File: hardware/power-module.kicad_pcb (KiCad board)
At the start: 2 copper layers, 33 x 82 mm, 35 parts, among them CN1 WJ2EDGRC-5.08-2P, K1 SRD-03VDC-SL-C, K2 SRD-03VDC-SL-C, K3 SRD-03VDC-SL-C, K4 SRD-03VDC-SL-C, Q1 BC547C, Q2 BC547C, U1 MIC5205-3.3YM5-MS, U2 PM254-2-05-W-8.5, U3 CC6903SO-10A, U4 ESP32-C3-MINI-1, U5 XC6206P332MR_C5148692

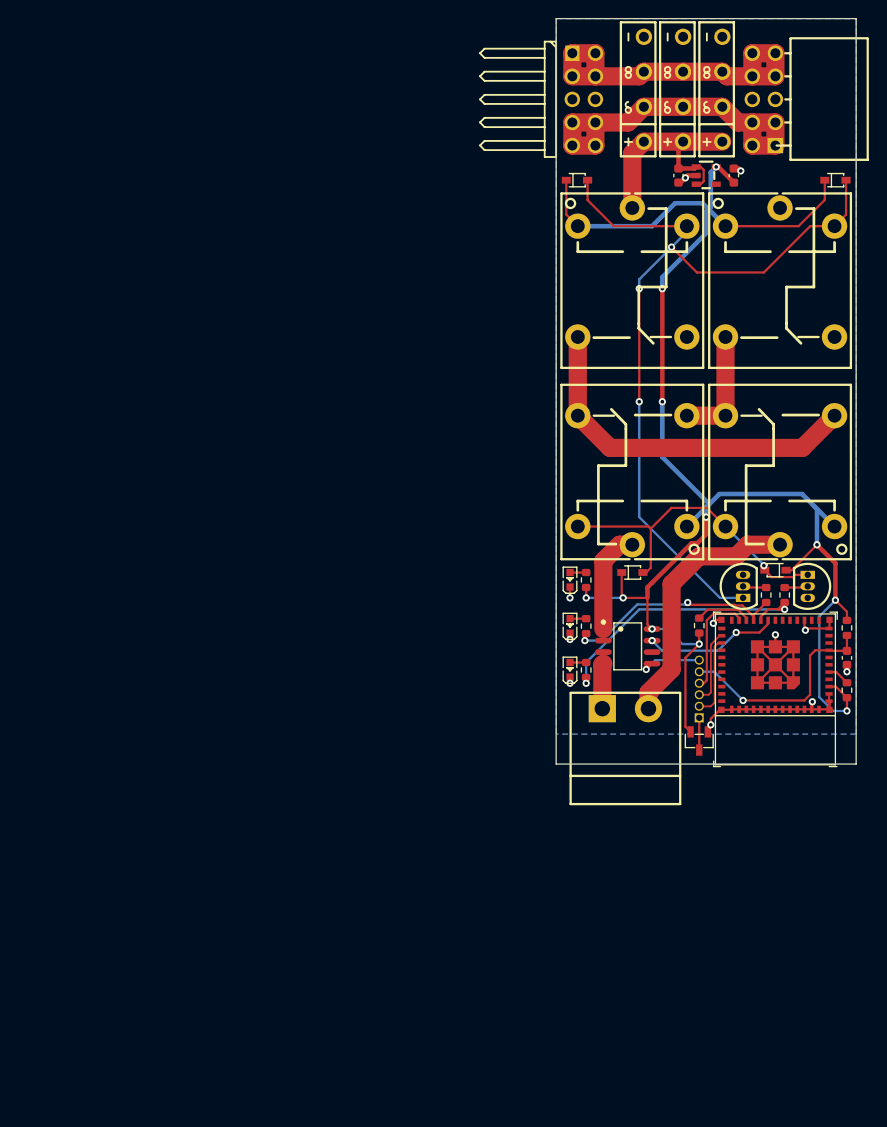
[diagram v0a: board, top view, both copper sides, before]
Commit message: Fix relay power supply, shrinked module to 1.5 DIN module widths
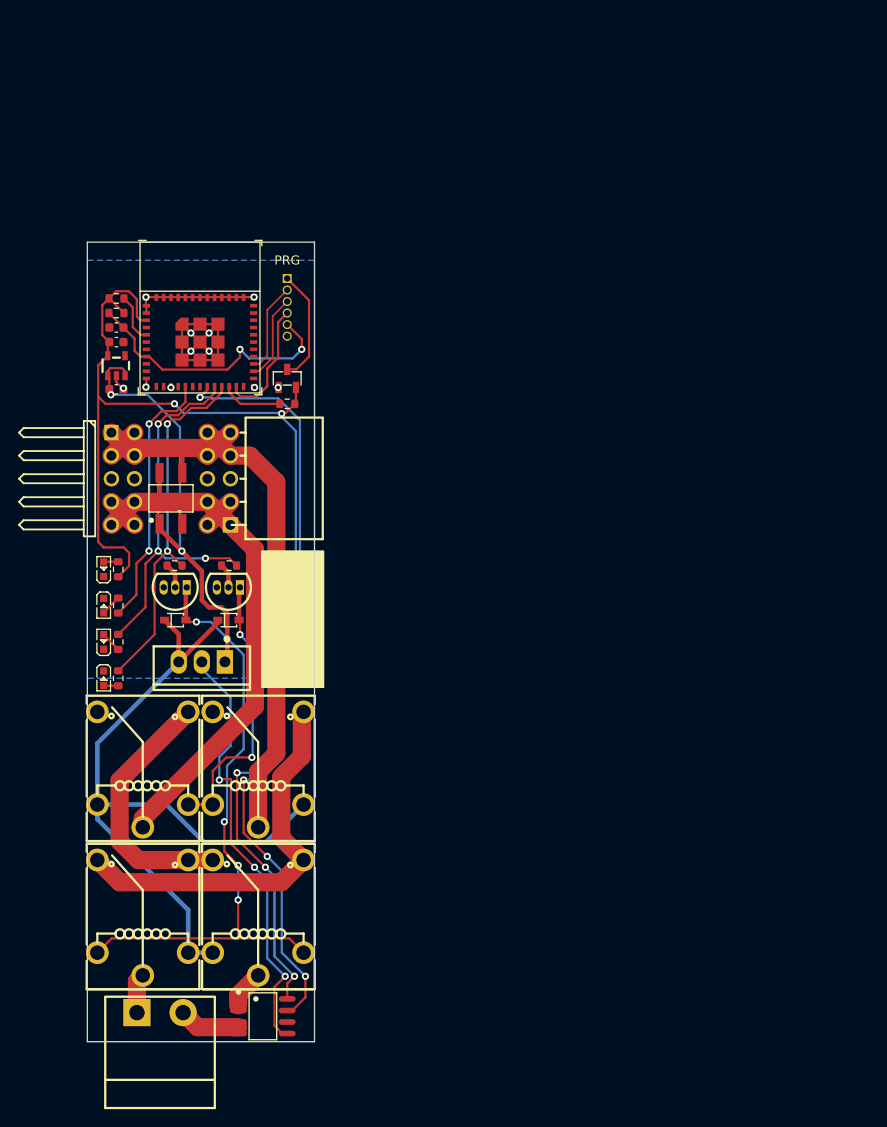
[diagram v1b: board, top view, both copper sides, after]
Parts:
- removed D4, D8: BAS321,115, easyeda2kicad:SOD-323_L1.8-W1.3-LS2.5-RD
- removed D6, D7: KBP307, easyeda2kicad:KBP_4P-L14.8-W3.8-P3.85-L
- removed K3, K4: SRD-03VDC-SL-C, easyeda2kicad:RELAY-TH_SRD-XXVDC-XL-C
- removed LED3: XL-1608UYC-06, easyeda2kicad:LED0603-RD-YELLOW
- removed Q2: BC547C, easyeda2kicad:TO-92-3_L4.9-W3.7-P1.27-L
- removed R2: 330, Resistor_SMD:R_0603_1608Metric
- removed R8: 120, Resistor_SMD:R_0603_1608Metric
- added K5: SRA-9VDC-CL, LCSC:RELAY-TH_SRA-9VDC-CL, F.Cu at (68.8, 124.3)
- added K6: SRA-9VDC-CL, LCSC:RELAY-TH_SRA-9VDC-CL, F.Cu at (56.1, 124.3)
- added LED4: XL-1608UYC-06, LCSC:LED0603-RD-YELLOW, F.Cu at (51.8, 90.0)
- added LED5: XL-1608UYC-06, LCSC:LED0603-RD-YELLOW, F.Cu at (51.8, 98.0)
- added Q3: BC547C, LCSC:TO-92-3_L4.9-W3.7-P1.27-L, F.Cu at (59.7, 88.0)
- added R10: 120, Resistor_SMD:R_0603_1608Metric, F.Cu at (53.4, 98.0)
- added R11: 330, Resistor_SMD:R_0603_1608Metric, F.Cu at (59.6, 85.6)
- added R9: 120, Resistor_SMD:R_0603_1608Metric, F.Cu at (53.4, 90.0)
- added U6: L7809CV_C347291, LCSC:TO-220-3_L10.0-W4.5-P2.54-L, F.Cu at (62.6, 96.2)
- CN1: footprint easyeda2kicad:CONN-TH_2P-P5.08_WJ2EDGRC-5.08-2P -> LCSC:CONN-TH_2P-P5.08_WJ2EDGRC-5.08-2P
- D1: value KBP307 -> MB10FH5G0NP; footprint easyeda2kicad:KBP_4P-L14.8-W3.8-P3.85-L -> LCSC:MBF_L4.8-W3.9-P2.50-LS6.7-TR
- D2, D3: footprint easyeda2kicad:SOD-323_L1.8-W1.3-LS2.5-RD -> LCSC:SOD-323_L1.8-W1.3-LS2.5-RD
- H1: footprint easyeda2kicad:HDR-TH_10P-P2.54-H-M-R2-C5-S2.54-W12.9 -> LCSC:HDR-TH_10P-P2.54-H-M-R2-C5-S2.54-W12.9
- H2: footprint easyeda2kicad:HDR-TH_6P-P1.27-V-M-A -> LCSC:HDR-TH_6P-P1.27-V-M-A
- K1, K2: value SRD-03VDC-SL-C -> SRA-9VDC-CL; footprint easyeda2kicad:RELAY-TH_SRD-XXVDC-XL-C -> LCSC:RELAY-TH_SRA-9VDC-CL
- LED1, LED2: footprint easyeda2kicad:LED0603-RD-YELLOW -> LCSC:LED0603-RD-YELLOW
- Q1: footprint easyeda2kicad:TO-92-3_L4.9-W3.7-P1.27-L -> LCSC:TO-92-3_L4.9-W3.7-P1.27-L
- U1: footprint easyeda2kicad:SOT-23-5_L2.9-W1.6-P0.95-LS2.8-BR -> LCSC:SOT-23-5_L2.9-W1.6-P0.95-LS2.8-BR
- U2: footprint easyeda2kicad:HDR-TH_10P-P2.54-H-F-R2-C5-W8.5 -> LCSC:HDR-TH_10P-P2.54-H-F-R2-C5-W8.5
- U3: footprint easyeda2kicad:SOP-8_L4.9-W3.9-P1.27-LS6.0-BL -> LCSC:SOP-8_L4.9-W3.9-P1.27-LS6.0-BL
- U5: footprint easyeda2kicad:SOT-23-3_L2.9-W1.3-P1.90-LS2.4-BR -> LCSC:SOT-23-3_L2.9-W1.3-P1.90-LS2.4-BR
- moved R5 91.2 mm to (53.2, 56.2), turned to 180 degrees
- moved C3 88.2 mm to (53.2, 59.4), turned to 0 degrees
- moved R4 87.6 mm to (53.2, 57.8), turned to 180 degrees
- moved K2 79.3 mm to (68.8, 108.0), turned to 90 degrees
- moved K1 76.8 mm to (56.1, 108.0), turned to 90 degrees
- moved U4 75.4 mm to (62.4, 58.3), turned to 0 degrees
- moved U2 73.1 mm to (64.5, 76.0)
- moved C2 70.4 mm to (53.2, 61.0), turned to 0 degrees
- moved D1 68.8 mm to (59.2, 78.2), turned to 180 degrees
- moved U1 68.2 mm to (53.2, 63.6), turned to -90 degrees
- moved D3 66.3 mm to (59.7, 91.6), turned to 0 degrees
- moved C1 66.2 mm to (53.2, 66.2), turned to 0 degrees
- moved H1 65.7 mm to (53.9, 76.0)
- moved H2 61.8 mm to (72.0, 57.2), turned to -90 degrees
- moved D2 61.8 mm to (65.5, 91.6)
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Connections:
- CN1 pad 1: Net-(CN1-Pad1) -> /TRACK OUT B
- CN1 pad 2: /TRACK POWER B -> Net-(CN1-Pad2)
- D1 pad 2: Net-(D1-AC-Pad2) -> /TRACK POWER A
- D1 pad 3: Net-(D1-AC-Pad3) -> GND
- D1 pad 4: GND -> /TRACK POWER B
- D2 pad 1: /CONTROLLER POWER IN -> /RELAY POWER
- D3 pad 1: /CONTROLLER POWER IN -> /RELAY POWER
- H1 pad 1: Net-(D1-AC-Pad3) -> /TRACK POWER B
- H1 pad 10: Net-(D1-AC-Pad2) -> /TRACK POWER A
- H1 pad 2: Net-(D1-AC-Pad3) -> /TRACK POWER B
- H1 pad 3: Net-(D1-AC-Pad3) -> /TRACK POWER B
- H1 pad 4: Net-(D1-AC-Pad3) -> /TRACK POWER B
- H1 pad 7: Net-(D1-AC-Pad2) -> /TRACK POWER A
- H1 pad 8: Net-(D1-AC-Pad2) -> /TRACK POWER A
- H1 pad 9: Net-(D1-AC-Pad2) -> /TRACK POWER A
- K1 pad 1: /CONTROLLER POWER IN -> /TRACK POWER A
- K1 pad 2: /TRACK POWER ENABLED + -> Net-(D2-A)
- K1 pad 3: unconnected-(K1-Pad3) -> /TRACK POWER ENABLED A
- K1 pad 4: Net-(D2-A) -> unconnected-(K1-Pad4)
- K1 pad 5: /TRACK POWER IN -> /RELAY POWER
- K2 pad 1: /CONTROLLER POWER IN -> /TRACK POWER B
- K2 pad 2: /TRACK POWER ENABLED - -> /RELAY POWER
- K2 pad 3: unconnected-(K2-Pad3) -> /TRACK POWER ENABLED B
- K2 pad 4: Net-(D2-A) -> unconnected-(K2-Pad4)
- K2 pad 5: GND -> Net-(D2-A)
- R1 pad 1: /TRACK POWER ENABLE -> Net-(Q1-B)
- R1 pad 2: Net-(Q1-B) -> /TRACK POWER ENABLE
- U2 pad 1: Net-(D1-AC-Pad2) -> /TRACK POWER A
- U2 pad 10: Net-(D1-AC-Pad3) -> /TRACK POWER B
- U2 pad 2: Net-(D1-AC-Pad2) -> /TRACK POWER A
- U2 pad 3: Net-(D1-AC-Pad2) -> /TRACK POWER A
- U2 pad 4: Net-(D1-AC-Pad2) -> /TRACK POWER A
- U2 pad 7: Net-(D1-AC-Pad3) -> /TRACK POWER B
- U2 pad 8: Net-(D1-AC-Pad3) -> /TRACK POWER B
- U2 pad 9: Net-(D1-AC-Pad3) -> /TRACK POWER B
- U3 pad 1: /TRACK POWER A -> /TRACK OUT A
- U3 pad 2: /TRACK POWER A -> /TRACK OUT A
- U3 pad 3: Net-(CN1-Pad1) -> Net-(CN1-Pad2)
- U3 pad 4: Net-(CN1-Pad1) -> Net-(CN1-Pad2)
- U4 pad 16: unconnected-(U4-GPIO10-Pad16) -> Net-(U4-GPIO10)
- U4 pad 20: /TRACK DIRECTION -> /TRACK POWER ENABLE
- U4 pad 21: /TRACK POWER ENABLE -> /TRACK DIRECTION
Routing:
- net /RELAY POWER: track 0.00 -> 80.4 mm
- net /CURRENT SENSING INPUT: track 15.4 -> 85.4 mm, vias 2 -> 4
- net Net-(D2-A): track 90.4 -> 30.7 mm, vias 3 -> 2
- net /TRACK POWER A: track 12.7 -> 65.2 mm
- net /CONTROLLER POWER IN: track 185.2 -> 140.0 mm, vias 11 -> 5
- net /TRACK POWER ENABLED B: track 0.00 -> 43.1 mm
- net /TRACK POWER B: track 28.7 -> 70.9 mm
- net /TRACK POWER ENABLED +: track 39.9 -> 0.00 mm
- net Net-(D1-AC-Pad2): track 39.0 -> 0.00 mm
- net Net-(D1-AC-Pad3): track 38.0 -> 0.00 mm
- net Net-(D3-A): track 35.6 -> 68.3 mm, vias 1 -> 4
- net GND: track 66.5 -> 97.4 mm, vias 12 -> 14
- net Net-(U4-GPIO10): track 0.00 -> 28.9 mm, vias 0 -> 2
- net /TRACK POWER ENABLED A: track 0.00 -> 28.5 mm
- net /TRACK POWER IN: track 25.1 -> 47.4 mm, vias 0 -> 2
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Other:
- board size 33 x 82 mm -> 25 x 88 mm
- board text added: "12V - 24V DC 8A"
- board text added: "PRG"
- board text added: "v2b"
- board text removed: "24V DC 9A"
- board text removed: "v1b"

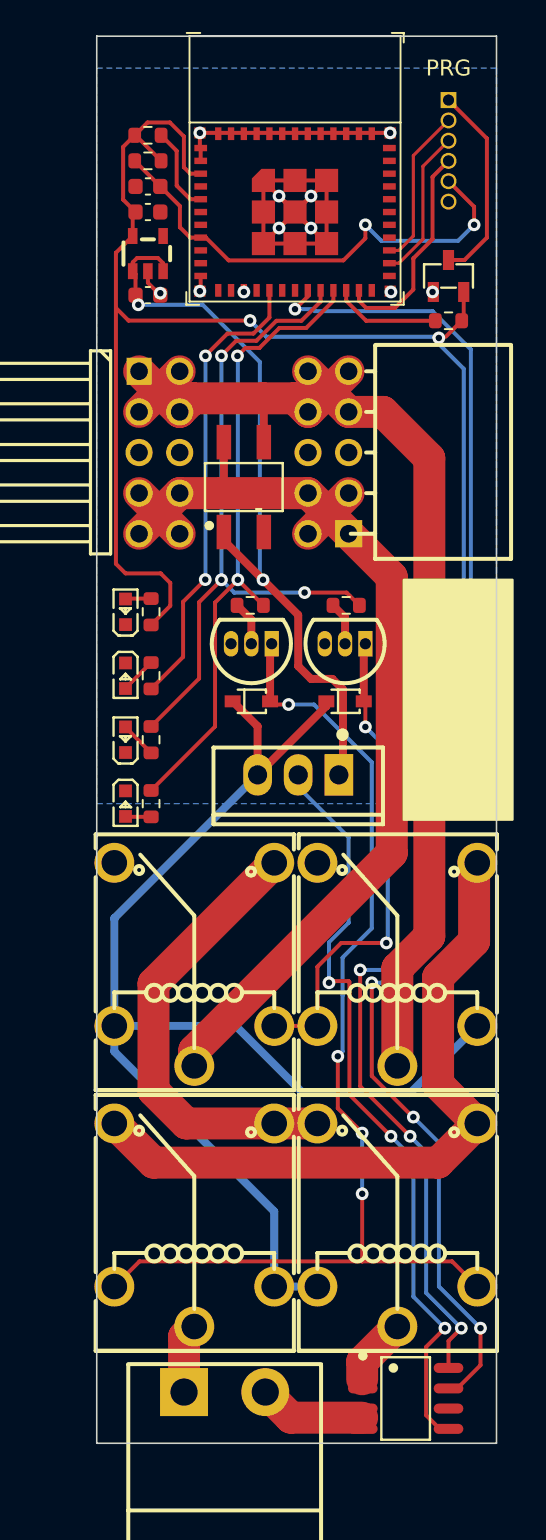
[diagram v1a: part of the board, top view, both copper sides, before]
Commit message: Add case slotting and holes
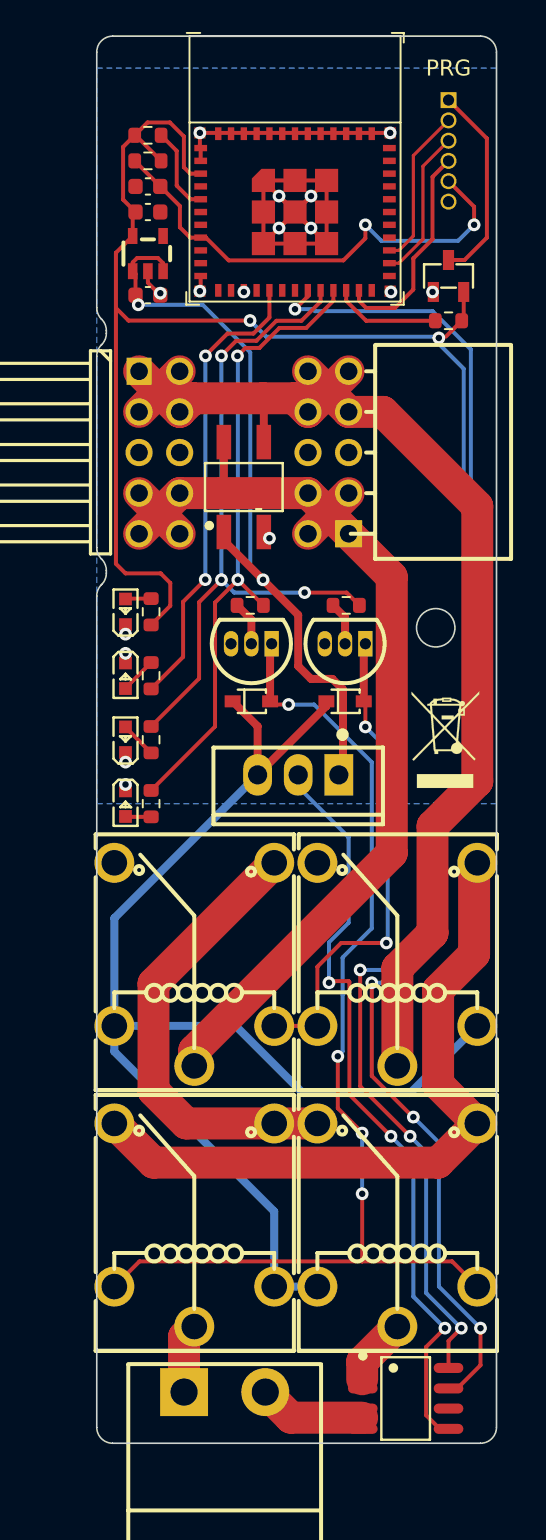
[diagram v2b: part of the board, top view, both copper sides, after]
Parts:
- added REF**: WEEE-Logo_4.2x6mm_SilkScreen, Symbol:WEEE-Logo_4.2x6mm_SilkScreen, F.Cu at (71.8, 94.0)
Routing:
- net GND: track 97.4 -> 100.1 mm, vias 14 -> 19
- net /TRACK POWER B: track 70.9 -> 73.4 mm
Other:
- outline, holes or cut-outs redrawn

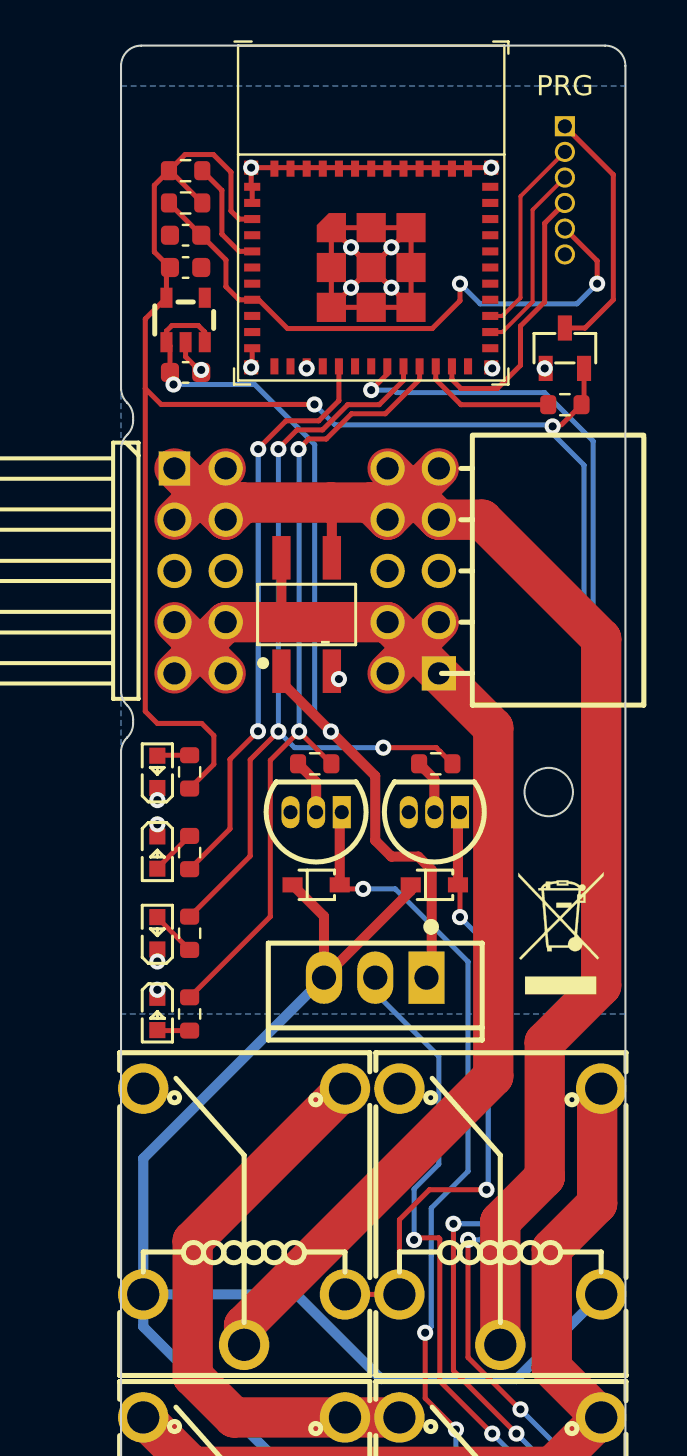
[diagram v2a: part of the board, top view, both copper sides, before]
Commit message: Fix relay switching transistors current rating
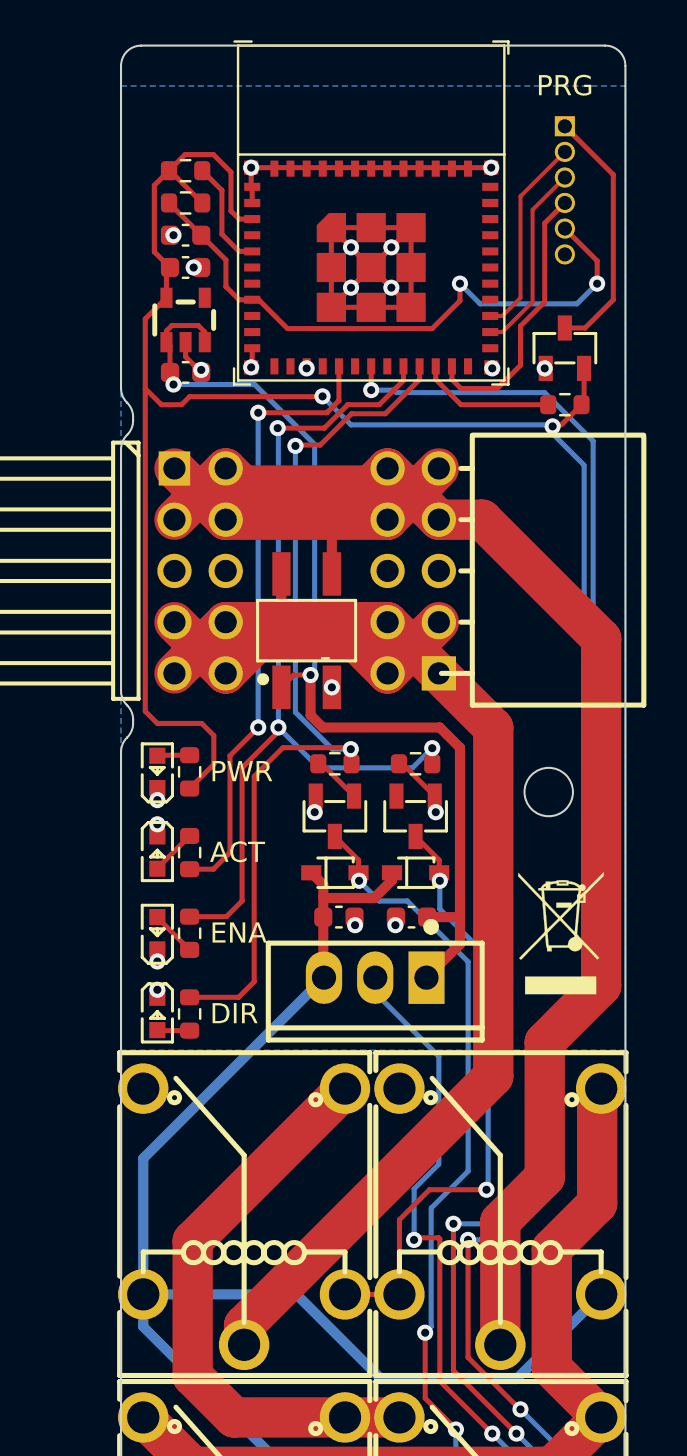
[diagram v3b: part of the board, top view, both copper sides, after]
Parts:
- removed Q3: BC547C, LCSC:TO-92-3_L4.9-W3.7-P1.27-L
- added C4: 330nF, Capacitor_SMD:C_0603_1608Metric, F.Cu at (64.4, 93.2)
- added C5: 100nF, Capacitor_SMD:C_0603_1608Metric, F.Cu at (60.8, 93.2)
- added Q2: SS8050_C2150, LCSC:SOT-23-3_L2.9-W1.3-P1.90-LS2.4-BR, F.Cu at (64.6, 88.2)
- Q1: value BC547C -> SS8050_C2150; footprint LCSC:TO-92-3_L4.9-W3.7-P1.27-L -> LCSC:SOT-23-3_L2.9-W1.3-P1.90-LS2.4-BR
- R1, R11: value 330 -> 560
- moved Q1 4.93 mm to (60.6, 88.2), turned to 90 degrees
- moved D2 1.11 mm to (64.6, 91.0)
- moved D3 1.11 mm to (60.6, 91.0)
- moved R1 1.00 mm to (64.6, 85.6)
- moved R11 1.00 mm to (60.6, 85.6)
- moved D1 0.80 mm to (59.2, 79.0)
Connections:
- Q1 pad 1: Net-(D2-A) -> Net-(Q1-B)
- Q1 pad 2: Net-(Q1-B) -> GND
- Q1 pad 3: GND -> Net-(D3-A)
- R1 pad 1: Net-(Q1-B) -> Net-(Q2-B)
- R11 pad 1: Net-(Q3-B) -> Net-(Q1-B)
- U4 pad 18: unconnected-(U4-GPIO4/ADC1_CH4-Pad18) -> /CURRENT SENSING INPUT
- U4 pad 19: /CURRENT SENSING INPUT -> unconnected-(U4-GPIO5/ADC2_CH0-Pad19)
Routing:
- net /TRACK POWER A: track 65.2 -> 82.8 mm
- net /TRACK POWER B: track 73.4 -> 90.2 mm
- net /TRACK DIRECTION: track 39.8 -> 44.7 mm
- net /TRACK POWER IN: track 47.4 -> 51.2 mm
- net Net-(Q2-B): track 0.00 -> 3.26 mm, vias 0 -> 1
- net Net-(Q3-B): track 2.77 -> 0.00 mm
- net /TRACK POWER ENABLE: track 42.6 -> 44.7 mm
- net /RELAY POWER: track 80.4 -> 78.4 mm
- net Net-(D3-A): track 68.3 -> 66.5 mm
- net Net-(U4-GPIO10): track 28.9 -> 30.7 mm
- net GND: track 100.1 -> 101.8 mm, vias 19 -> 24
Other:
- board text added: "ACT"
- board text added: "DIR"
- board text added: "ENA"
- board text added: "PWR"

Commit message: Add wifi version
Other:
- board text added: "8A = 70°C"
